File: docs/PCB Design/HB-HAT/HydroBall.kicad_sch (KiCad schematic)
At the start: 62 parts, among them IC1 HIH8130-021-001, J1 Conn_01x05, J11 Conn_02x05_Top_Bottom, J13 Conn_01x06, J14 Conn_02x04_Counter_Clockwise, J2 Conn_01x07, J3 Conn_01x05, J4 Conn_01x05, J5 Conn_01x06, J6 Conn_01x05, J7 Conn_01x05, J8 Raspberry_Pi_2_3, J9 Conn_01x03, Q2 2N7000, U4 INA238AIDGSR, U7 PCA9533DP_02,118, U8 DS3231MZ

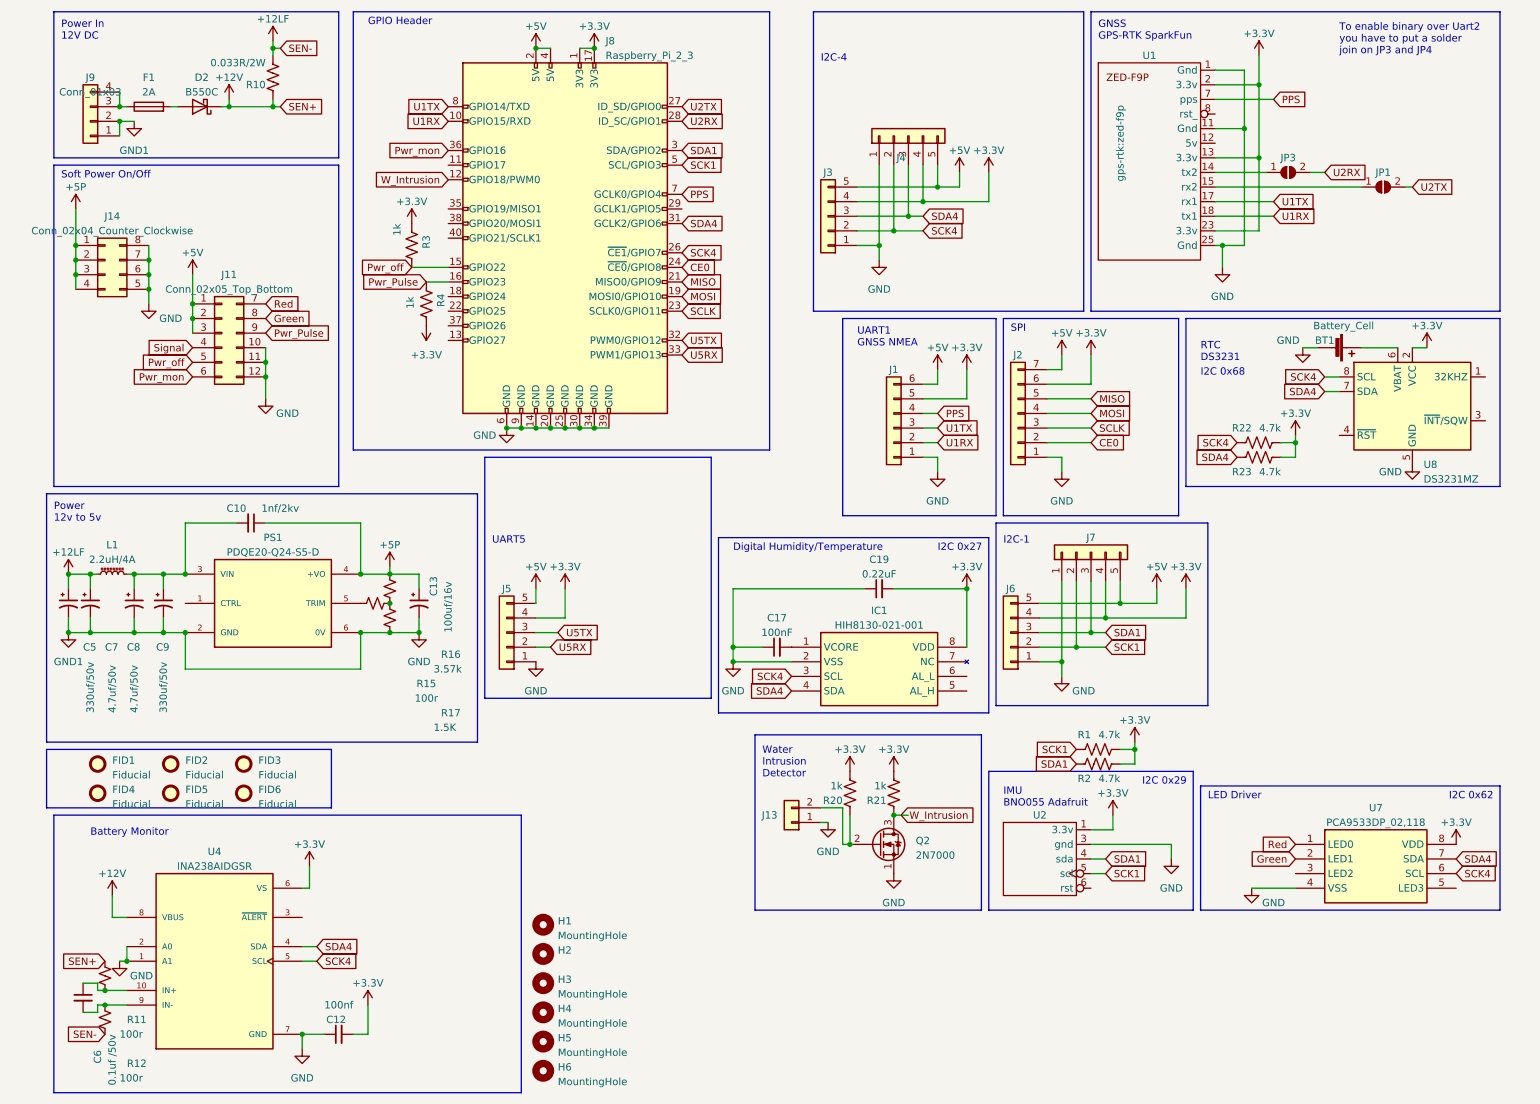
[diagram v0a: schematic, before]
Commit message: PCB : HB-HAT replace led driver by mosfet connected on gpio
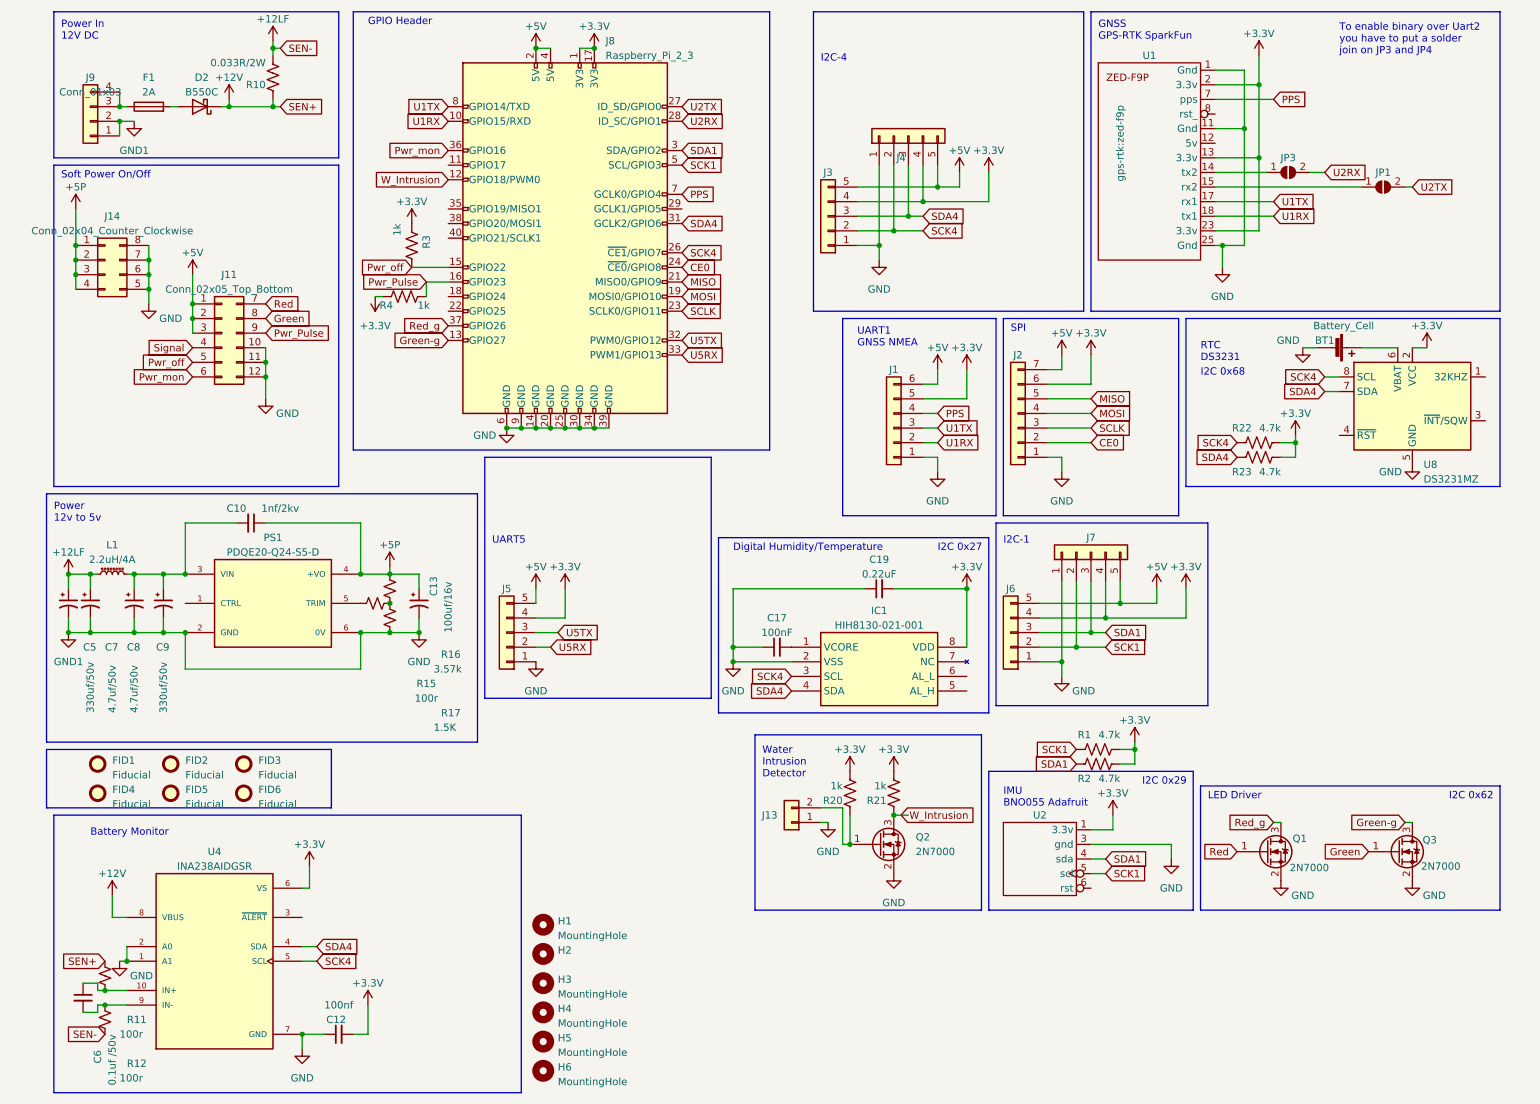
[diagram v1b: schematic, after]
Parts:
- removed U7: PCA9533DP_02,118, KiCad:SOIC127P600X175-8N, symbol PCA9533DP_02_118:PCA9533DP_02,118
- added Q1, Q3: 2N7000, Package_TO_SOT_SMD:SOT-23, symbol Transistor_FET:2N7002
- Q2: footprint Package_TO_SOT_SMD:SOT-23-3 -> Package_TO_SOT_SMD:SOT-23; symbol Transistor_FET:2N7000 -> Transistor_FET:2N7002
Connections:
- net +3.3V: now also R4.2; no longer R4.1
- net GND: now also Q2.2 (S), Q1.2 (S), Q3.2 (S); no longer Q2.1 (S)
- net Green: now also Q3.1 (G)
- net Pwr_Pulse: now also R4.1; no longer R4.2
- net Red: now also Q1.1 (G)
- net at J13.2 (Pin_2), R20.1: now also Q2.1 (G); no longer Q2.2 (G)
- net Green-g: now reaches J8.13 (GPIO27)
- net Green-g: now also Q3.3 (D)
- net Red_g: now reaches J8.37 (GPIO26)
- net Red_g: now also Q1.3 (D)
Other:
- moved on the sheet: R4

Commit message: DC to DC converter replacement with filtration and voltage correction TBC.
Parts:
- C10: value 1nf/2kv -> 4.7nf/2kv
- C13: value 100uf/16v -> DNP
- C5: value 330uf/50v -> 150uf/50v
- C7: value 4.7uf/50v -> DNP
- C8: value 4.7uf/50v -> 10uf/50v
- C9: value 330uf/50v -> 47uf/50v
- L1: value 2.2uH/4A -> 22uH/4A
- PS1: value PDQE20-Q24-S5-D -> REC20K-2405SZ
- R15: value 100r -> 0R
- R16: value 3.57k -> DNP
- R17: value 1.5K -> 169K
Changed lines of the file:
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@@
 			)
 		)
-		(property "Value" "330uf/50v"
+		(property "Value" "47uf/50v"
 			(at 33.02 135.89 90)
 			(effects
@@
 			)
 		)
-		(property "Value" "4.7uf/50v"
+		(property "Value" "10uf/50v"
 			(at 27.94 135.89 90)
 			(effects
@@
 			)
 		)
-		(property "Value" "1nf/2kv"
+		(property "Value" "4.7nf/2kv"
 			(at 53.34 100.33 90)
 			(effects
@@
 			)
 		)
-		(property "Value" "100uf/16v"
+		(property "Value" "DNP"
 			(at 82.55 121.92 90)
 			(effects
@@
 		(fields_autoplaced yes)
 		(property "Reference" "PS1"
-			(at 52.07 105.41 0)
+			(at 52.07 104.14 0)
 			(effects
 				(font
@@
 			)
 		)
-		(property "Value" "PDQE20-Q24-S5-D"
-			(at 52.07 107.95 0)
+		(property "Value" "REC20K-2405SZ"
+			(at 52.07 106.68 0)
 			(effects
 				(font
@@
 		(fields_autoplaced yes)
 		(property "Reference" "L1"
-			(at 24.13 106.68 90)
+			(at 24.13 105.41 90)
 			(effects
 				(font
@@
 			)
 		)
-		(property "Value" "2.2uH/4A"
-			(at 24.13 109.22 90)
+		(property "Value" "22uH/4A"
+			(at 24.13 107.95 90)
 			(effects
 				(font
@@
 			)
 		)
-		(property "Value" "3.57k"
+		(property "Value" "DNP"
 			(at 80.01 128.27 0)
 			(effects
@@
 			)
 		)
-		(property "Value" "330uf/50v"
+		(property "Value" "150uf/50v"
 			(at 20.32 135.89 90)
 			(effects
@@
 			)
 		)
-		(property "Value" "1.5K"
+		(property "Value" "169K"
 			(at 80.01 138.43 0)
 			(effects
@@
 			)
 		)
-		(property "Value" "4.7uf/50v"
+		(property "Value" "DNP"
 			(at 24.13 135.89 90)
 			(effects
@@
 			)
 		)
-		(property "Value" "100r"
+		(property "Value" "0R"
 			(at 78.74 133.35 90)
 			(effects

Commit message: PCB HB-HAT : fix mosfet pinout
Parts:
- Q1, Q2, Q3: value 2N7000 -> 2N7002
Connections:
- net Red: now also Q2.1 (G); no longer Q1.1 (G)
- net Red_g: now also Q2.3 (D); no longer Q1.3 (D)
- net W_Intrusion: now also Q1.3 (D); no longer Q2.3 (D)
- net at J13.2 (Pin_2), R20.1: now also Q1.1 (G); no longer Q2.1 (G)
